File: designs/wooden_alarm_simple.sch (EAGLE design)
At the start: 16 parts, among them IC1 ESP-12E/F

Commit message: printready alarm simple layout
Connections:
- net GND: now also JUMPER_CLK.2; no longer JUMPER_CLK.1
- net VCC: now also JUMPER_CLK.1; no longer JUMPER_CLK.2
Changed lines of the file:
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@@
-</segment>
-<segment>
-<pinref part="JUMPER_CLK" gate="1" pin="2"/>
-<wire x1="33.02" y1="38.1" x2="34.29" y2="38.1" width="0.1524" layer="91"/>
-<label x="34.29" y="38.1" size="1.778" layer="95"/>
 </segment>
 <segment>
@@
 <wire x1="119.38" y1="-10.16" x2="119.38" y2="-7.62" width="0.1524" layer="91"/>
 <label x="119.38" y="-7.62" size="1.778" layer="95" rot="R90"/>
+</segment>
+<segment>
+<pinref part="JUMPER_CLK" gate="1" pin="1"/>
+<wire x1="33.02" y1="35.56" x2="34.29" y2="35.56" width="0.1524" layer="91"/>
+<label x="33.02" y="35.56" size="1.778" layer="95"/>
 </segment>
 </net>
@@
 </segment>
 <segment>
-<pinref part="JUMPER_CLK" gate="1" pin="1"/>
-<wire x1="33.02" y1="35.56" x2="34.29" y2="35.56" width="0.1524" layer="91"/>
-<label x="34.29" y="35.56" size="1.778" layer="95"/>
-</segment>
-<segment>
 <pinref part="IO_0_SWITCH" gate="G$1" pin="3"/>
 <wire x1="210.82" y1="15.24" x2="210.82" y2="22.86" width="0.1524" layer="91"/>
@@
 <label x="121.92" y="-7.62" size="1.778" layer="95" rot="R90"/>
 </segment>
+<segment>
+<pinref part="JUMPER_CLK" gate="1" pin="2"/>
+<wire x1="33.02" y1="38.1" x2="34.29" y2="38.1" width="0.1524" layer="91"/>
+<label x="33.02" y="38.1" size="1.778" layer="95"/>
+</segment>
 </net>

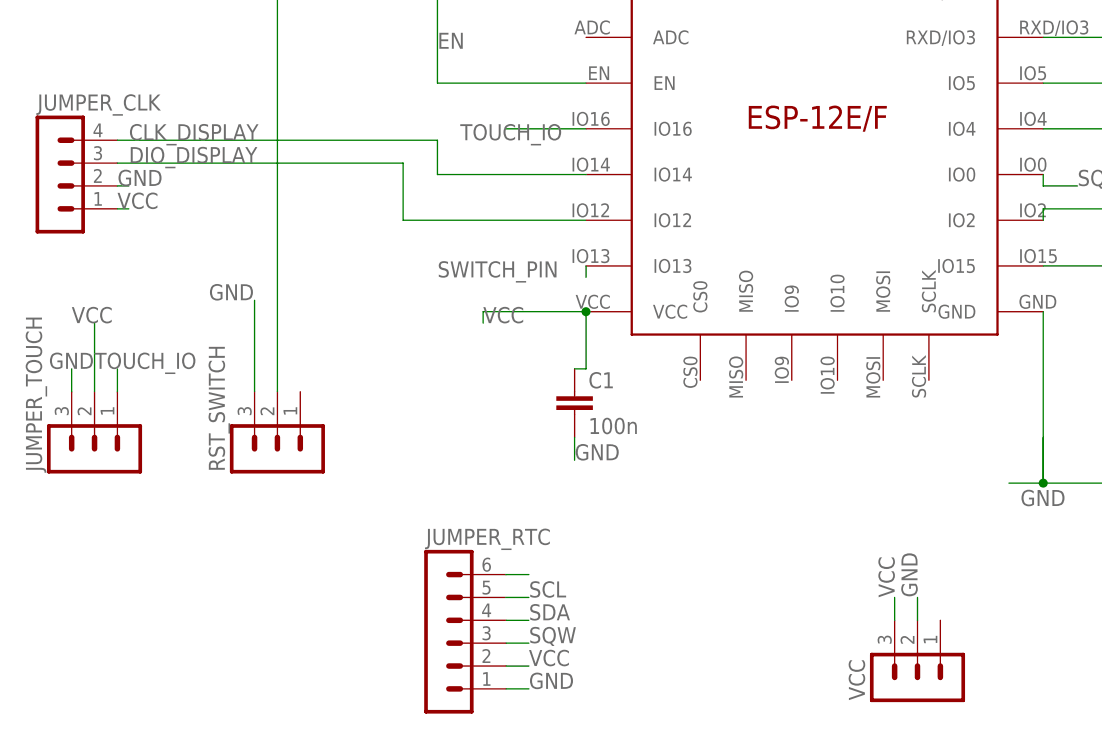
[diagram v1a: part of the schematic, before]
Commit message: updated layout and pdf for etching
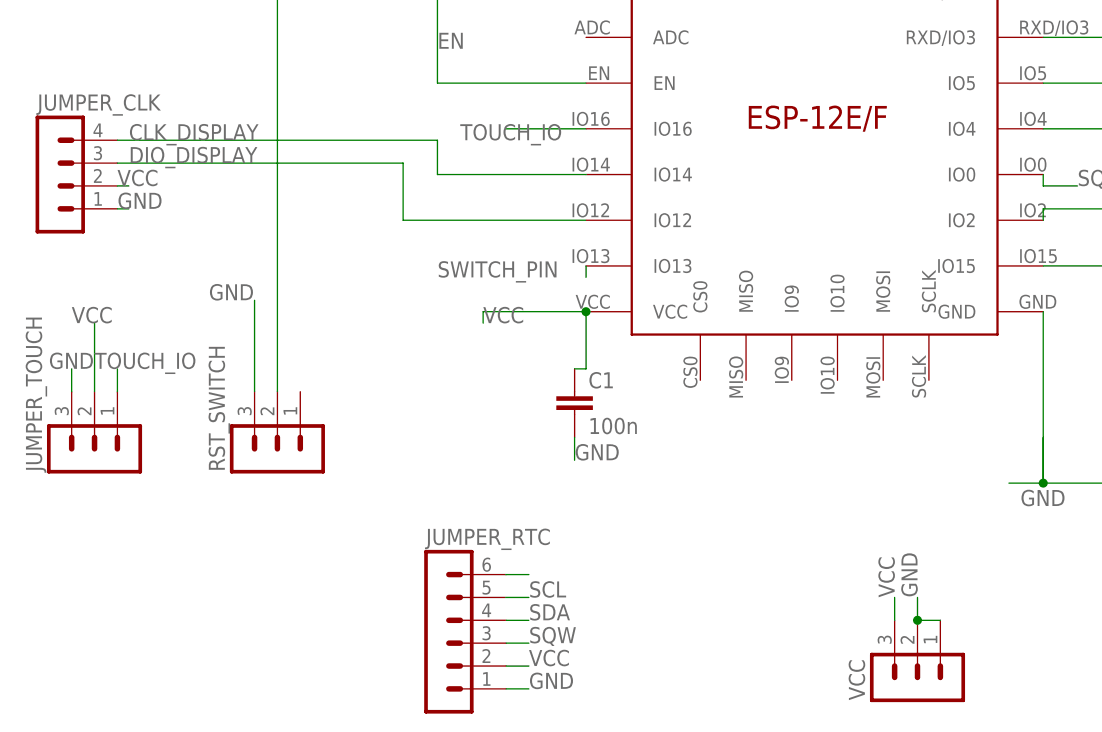
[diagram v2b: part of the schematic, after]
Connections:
- net GND: now also JUMPER_CLK.1, VCC.1; no longer JUMPER_CLK.2
- net VCC: now also JUMPER_CLK.2; no longer JUMPER_CLK.1
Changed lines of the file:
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@@
 </segment>
 <segment>
-<pinref part="JUMPER_CLK" gate="1" pin="1"/>
-<wire x1="33.02" y1="35.56" x2="34.29" y2="35.56" width="0.1524" layer="91"/>
-<label x="33.02" y="35.56" size="1.778" layer="95"/>
+<pinref part="JUMPER_CLK" gate="1" pin="2"/>
+<wire x1="33.02" y1="38.1" x2="34.29" y2="38.1" width="0.1524" layer="91"/>
+<label x="33.02" y="38.1" size="1.778" layer="95"/>
 </segment>
 </net>
@@
 <wire x1="121.92" y1="-10.16" x2="121.92" y2="-7.62" width="0.1524" layer="91"/>
 <label x="121.92" y="-7.62" size="1.778" layer="95" rot="R90"/>
+<pinref part="VCC" gate="G$1" pin="1"/>
+<wire x1="124.46" y1="-10.16" x2="121.92" y2="-10.16" width="0.1524" layer="91"/>
+<junction x="121.92" y="-10.16"/>
 </segment>
 <segment>
-<pinref part="JUMPER_CLK" gate="1" pin="2"/>
-<wire x1="33.02" y1="38.1" x2="34.29" y2="38.1" width="0.1524" layer="91"/>
-<label x="33.02" y="38.1" size="1.778" layer="95"/>
+<pinref part="JUMPER_CLK" gate="1" pin="1"/>
+<wire x1="33.02" y1="35.56" x2="34.29" y2="35.56" width="0.1524" layer="91"/>
+<label x="33.02" y="35.56" size="1.778" layer="95"/>
 </segment>
 </net>
